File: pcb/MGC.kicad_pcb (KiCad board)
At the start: 2 copper layers, 92.7 x 62.2 mm, 121 parts, among them J1 USB_C_Receptacle, J10 Conn_01x04_Pin, J11 103R012BB100, J12 103R012BB100, J13 103R012BB100, J14 Conn_02x10_Odd_Even, J15 Conn_02x10_Odd_Even, J16 Conn_01x03, J17 Conn_01x01_Pin, J18 Conn_01x02_Pin, J19 Conn_01x02_Pin, J2 Conn_01x02_Pin, J20 Conn_01x02_Pin, J3 103R012BB100, J4 Conn_02x03_Odd_Even, J5 Conn_02x05_Odd_Even, J6 Conn_01x04, J7 103R012BB100, J8 Conn_01x01_Pin, J9 Conn_01x01_Pin, Q10 AO3400A, Q11 AO3400A, Q12 AO3400A, Q13 AO3400A, Q9 AO3400A, SW0 SW_SPST, SW1 SW_SPST, SW2 SW_SPST, SW3 SW_SPST, SW5 SW_SPST, SW6 SW_DIP_x02, U1 FT230XS, U2 TS3USB30EDGSR, U3 74AHC1G14, U4 TPS2116DRL, U5 LM1117DT-3.3, U6 TBD62783A, U7 MB85RC04V

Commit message: Optimize fabrication layer
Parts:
- C10, C9: value 100u -> 10u
- D0, D1, D10, D11, D2, D3, D4, D5: value LED -> Green
- D12, D6: value LED -> Yellow
- D7, D9: value LED -> Red
- F1: value 2.0A -> 350mA
- R33, R35, R7: value 560 -> 150

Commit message: Adapt device values
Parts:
- C10, C11, C3, C7, C9: value 10u -> 100u
- F1: value 350mA -> 1A
- R1, R2, R3, R38, R4, R5, R6: value 560 -> 270
- R39: value 560 -> 150
- R7: value 150 -> 330
- R8: value 560 -> 330
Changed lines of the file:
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@@
 			)
 		)
-		(property "Value" "560"
+		(property "Value" "270"
 			(at 3.556 0 90)
 			(layer "F.Fab")
@@
 			)
 		)
-		(property "Value" "10u"
+		(property "Value" "100u"
 			(at 0 2.35 90)
 			(layer "F.Fab")
@@
 			)
 		)
-		(property "Value" "560"
+		(property "Value" "270"
 			(at 3.556 0 90)
 			(layer "F.Fab")
@@
 			)
 		)
-		(property "Value" "560"
+		(property "Value" "330"
 			(at 3.556 0 90)
 			(layer "F.Fab")
@@
 			)
 		)
-		(property "Value" "560"
+		(property "Value" "270"
 			(at 3.556 0 90)
 			(layer "F.Fab")
@@
 			)
 		)
-		(property "Value" "560"
+		(property "Value" "270"
 			(at 3.556 0 90)
 			(layer "F.Fab")
@@
 			)
 		)
-		(property "Value" "10u"
+		(property "Value" "100u"
 			(at 0 2.35 0)
 			(layer "F.Fab")
@@
 			)
 		)
-		(property "Value" "10u"
+		(property "Value" "100u"
 			(at 0 -2.54 90)
 			(layer "F.Fab")
@@
 			)
 		)
-		(property "Value" "150"
+		(property "Value" "330"
 			(at 3.556 0 90)
 			(layer "F.Fab")
@@
 			)
 		)
-		(property "Value" "10u"
-			(at 3.556 0 90)
+		(property "Value" "100u"
+			(at 3.937 0 90)
 			(layer "F.Fab")
 			(effects
@@
 			)
 		)
-		(property "Value" "560"
+		(property "Value" "270"
 			(at 3.556 0 90)
 			(layer "F.Fab")
@@
 			)
 		)
-		(property "Value" "10u"
+		(property "Value" "100u"
 			(at -4.629 0 90)
 			(layer "F.Fab")
@@
 			)
 		)
-		(property "Value" "560"
+		(property "Value" "270"
 			(at 3.556 0 90)
 			(layer "F.Fab")
@@
 			)
 		)
-		(property "Value" "350mA"
+		(property "Value" "1A"
 			(at 0 -1.83 0)
 			(layer "B.Fab")
@@
 			)
 		)
-		(property "Value" "560"
+		(property "Value" "150"
 			(at 3.2405 0 0)
 			(layer "B.Fab")
@@
 			)
 		)
-		(property "Value" "560"
+		(property "Value" "270"
 			(at -3.7145 0 0)
 			(layer "B.Fab")

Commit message: Add missing vendor(id)
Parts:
- C9: value 100u -> 47u
- D14, D15: value 1N4148 -> BAT43
- Q10, Q11, Q12, Q13, Q9: value AO3400A -> AO3416

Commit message: Fix connector pin direction
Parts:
- FID1: footprint Images:QR_0x007e_small -> Images:QR_0x007e_very_small
- J10: footprint Connector_PinSocket_2.54mm:PinSocket_1x04_P2.54mm_Vertical_SMD_Pin1Left -> Connector_PinSocket_2.54mm:PinSocket_1x04_P2.54mm_Vertical_SMD_Pin1Right
- J18, J19, J2, J20: footprint Connector_PinHeader_2.54mm:PinHeader_1x02_P2.54mm_Vertical_SMD_Pin1Left -> Connector_PinHeader_2.54mm:PinHeader_1x02_P2.54mm_Vertical_SMD_Pin1Right
- moved FID3 20.5 mm to (190.1, 88.5)
- moved R51 15.3 mm to (159.2, 79.8)
- moved R49 4.06 mm to (174.4, 82.0)
- moved FID1 2.06 mm to (164.3, 79.2)
- moved R48 1.50 mm to (152.1, 93.2), turned to 180 degrees
- moved Q13 1.22 mm to (159.7, 82.9), turned to -90 degrees
- moved J10 1.13 mm to (181.8, 90.2)
- moved J18 0.39 mm to (157.5, 94.9)
- moved J19 0.10 mm to (180.1, 80.4), turned to -90 degrees
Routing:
- net Net-(Q13-G): track 19.6 -> 14.6 mm
- net PWM: track 6.46 -> 2.77 mm
- net PROG_IN: track 38.3 -> 34.9 mm
- net V_POT: track 16.4 -> 19.7 mm
- net Net-(J20-Pin_1): track 12.1 -> 15.4 mm
- net TONE: track 36.7 -> 33.8 mm
- net /PROG_7: track 14.3 -> 16.9 mm
- net Net-(J19-Pin_1): track 2.92 -> 5.46 mm
- net PROG_OUT: track 33.4 -> 35.9 mm
- net Net-(Q12-G): track 5.86 -> 4.06 mm
- net /PROG_10: track 23.8 -> 25.6 mm
- net Net-(BZ1--): track 6.99 -> 8.71 mm
- net Net-(J18-Pin_1): track 3.81 -> 2.69 mm
- net /GPIO/PC1: track 57.3 -> 56.4 mm
- net /PROG_9: track 14.3 -> 14.8 mm, vias 1 -> 3
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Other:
- outline, holes or cut-outs redrawn
- board text added: "EXT"
- board text removed: "SPECIAL"

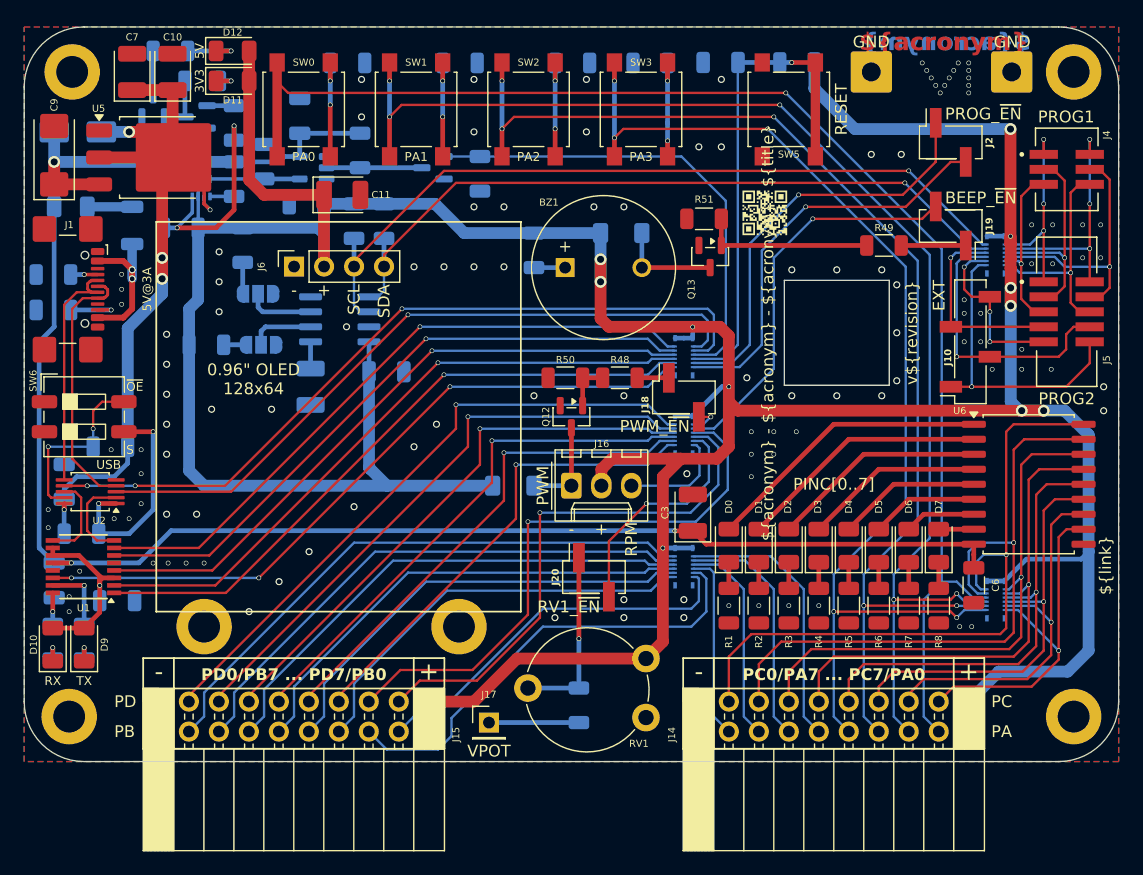
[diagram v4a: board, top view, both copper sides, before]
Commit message: Add dimensioning
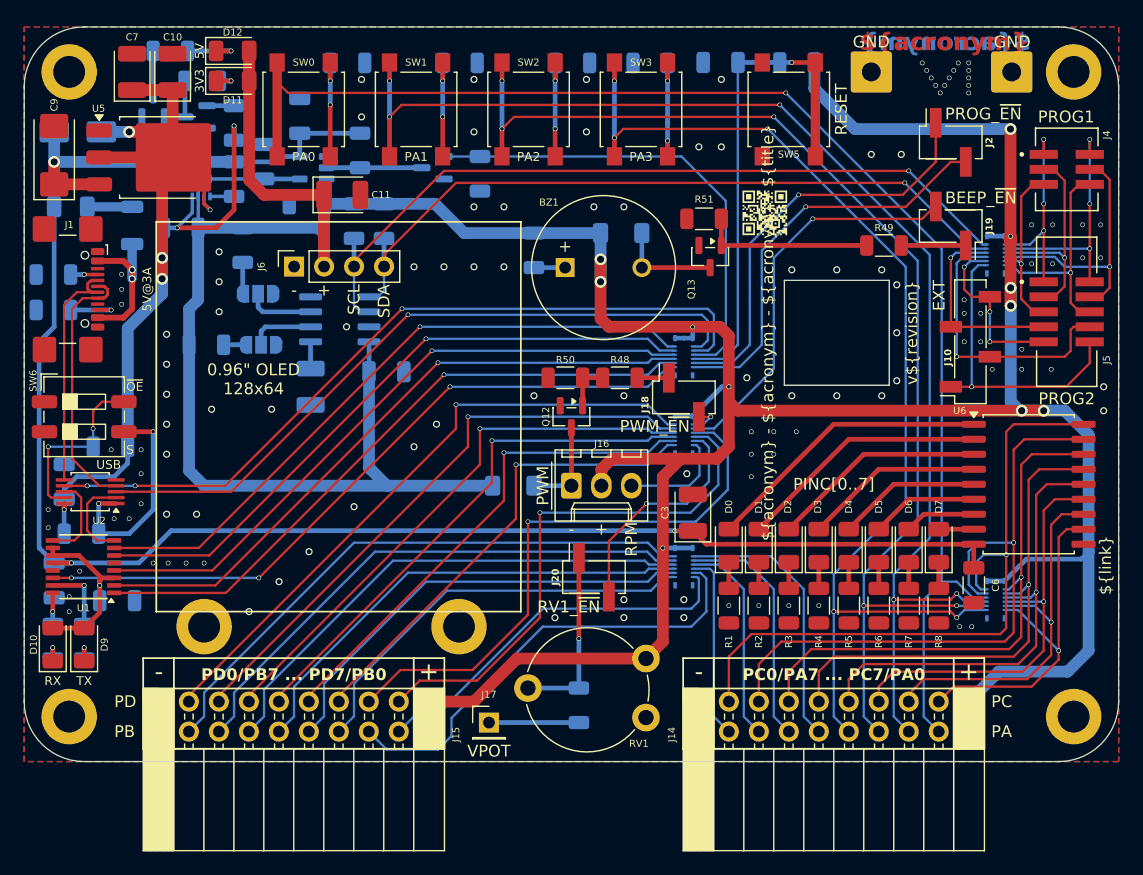
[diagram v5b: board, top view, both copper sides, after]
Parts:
- moved H3 0.26 mm to (105.4, 67.3)
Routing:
- net VDD: track 348.6 -> 349.2 mm
